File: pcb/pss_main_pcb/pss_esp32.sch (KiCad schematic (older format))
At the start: 17 parts, among them J6 UART_Prog, SW4 Main Encoder Input, SW5 EN, SW6 Boot, U6 ESP32-WROOM-32U, U7 2.8inch_SPI_Module_ILI9341_SK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

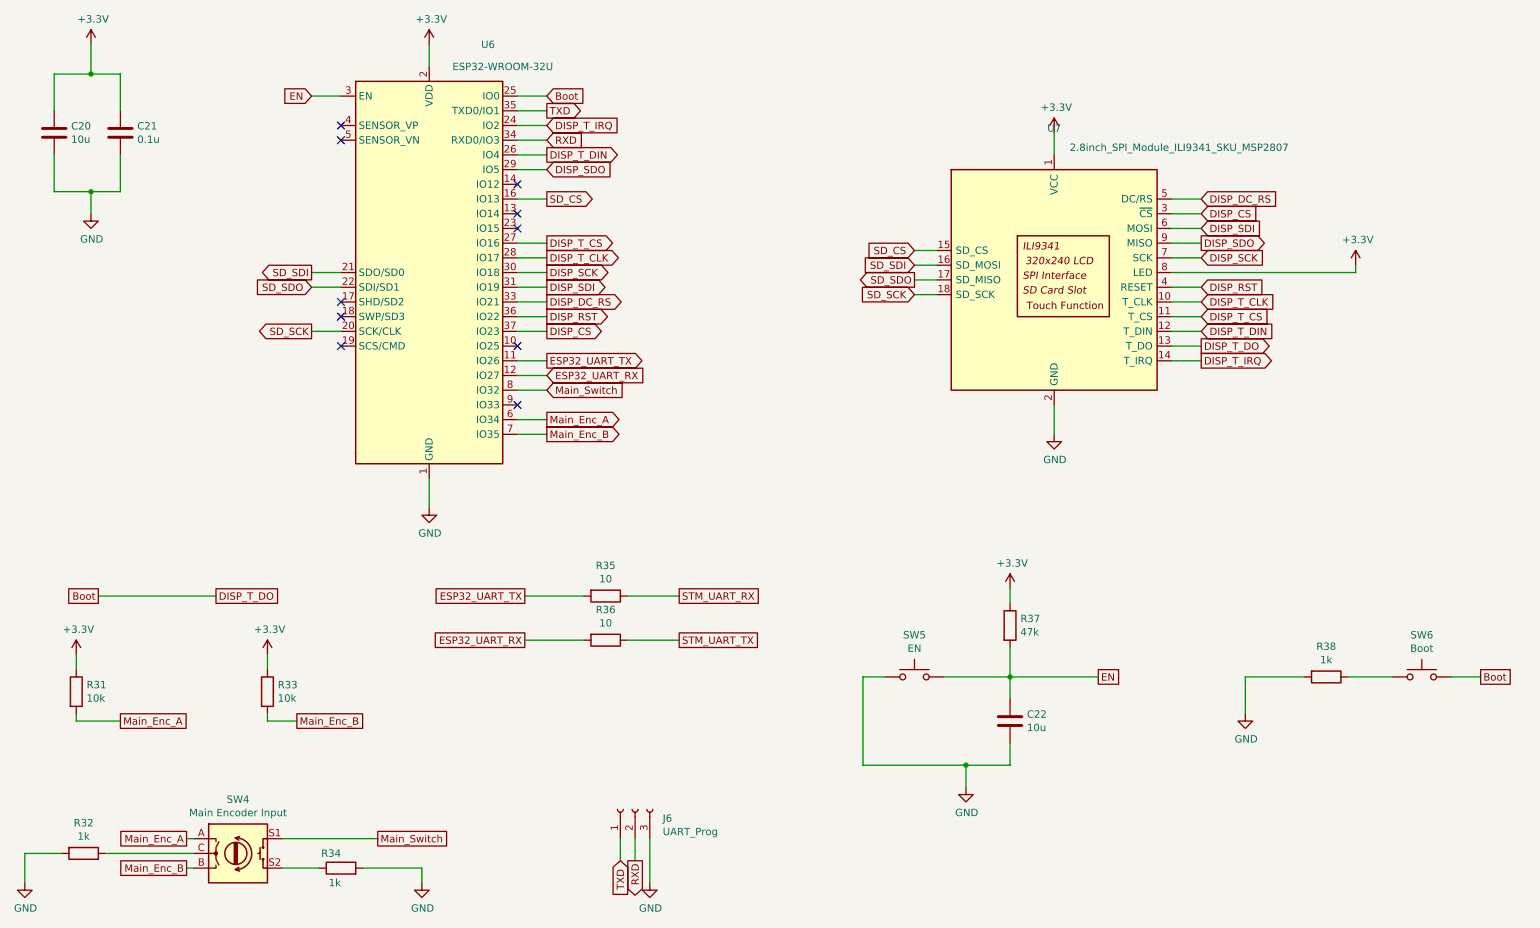
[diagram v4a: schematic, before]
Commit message: Change footprints
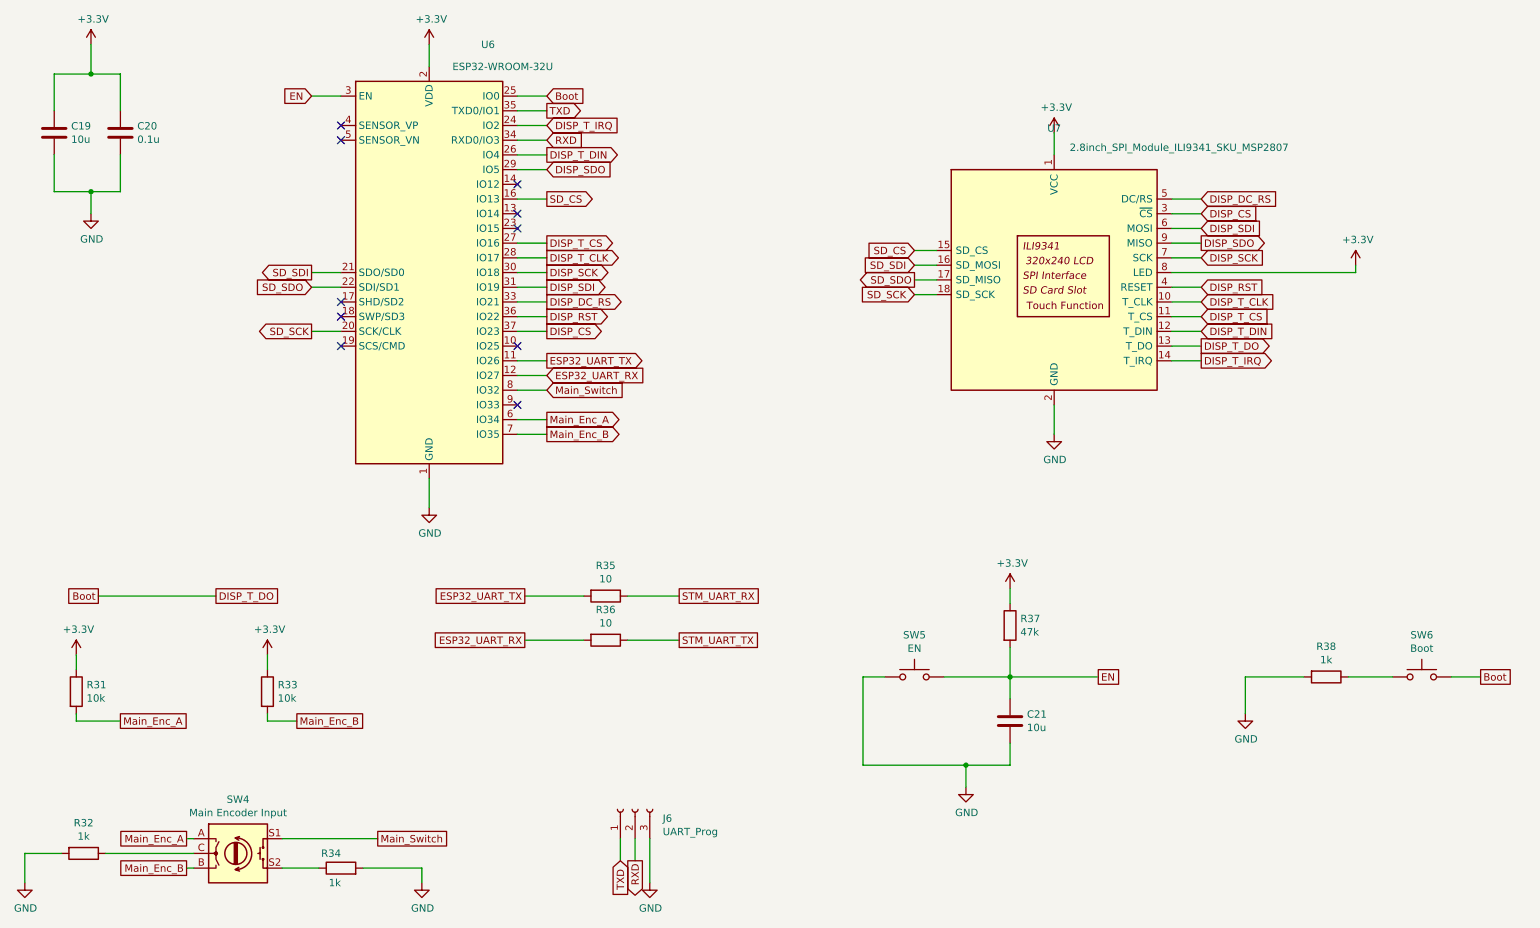
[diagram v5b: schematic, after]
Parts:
- renumbered C20 to C19, C21 to C20, C22 to C21
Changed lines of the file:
@@
 AR Path="/5EE027BC/5ED3F917" Ref="#PWR?"  Part="1"
 AR Path="/5EE5A305/5ED3F917" Ref="#PWR?"  Part="1"
-AR Path="/5ED3D5DF/5ED3F917" Ref="#PWR0147"  Part="1"
-F 0 "#PWR0147" H 750 6600 50  0001 C CNN
+AR Path="/5ED3D5DF/5ED3F917" Ref="#PWR049"  Part="1"
+F 0 "#PWR049" H 750 6600 50  0001 C CNN
 F 1 "GND" H 755 6677 50  0000 C CNN
 F 2 "" H 750 6850 50  0001 C CNN
@@
 AR Path="/5EE027BC/5ED3F923" Ref="#PWR?"  Part="1"
 AR Path="/5EE5A305/5ED3F923" Ref="#PWR?"  Part="1"
-AR Path="/5ED3D5DF/5ED3F923" Ref="#PWR0148"  Part="1"
-F 0 "#PWR0148" H 3450 6600 50  0001 C CNN
+AR Path="/5ED3D5DF/5ED3F923" Ref="#PWR054"  Part="1"
+F 0 "#PWR054" H 3450 6600 50  0001 C CNN
 F 1 "GND" H 3455 6677 50  0000 C CNN
 F 2 "" H 3450 6850 50  0001 C CNN
@@
 	750  6650 1000 6650
 $Comp
-L power:+3.3V #PWR0149
+L power:+3.3V #PWR055
 U 1 1 5ED5E5AE
 P 3500 1150
-F 0 "#PWR0149" H 3500 1000 50  0001 C CNN
+F 0 "#PWR055" H 3500 1000 50  0001 C CNN
 F 1 "+3.3V" H 3515 1323 50  0000 C CNN
 F 2 "" H 3500 1150 50  0001 C CNN
@@
 	3500 1300 3500 1150
 $Comp
-L power:GND #PWR0150
+L power:GND #PWR056
 U 1 1 5ED5F238
 P 3500 4300
-F 0 "#PWR0150" H 3500 4050 50  0001 C CNN
+F 0 "#PWR056" H 3500 4050 50  0001 C CNN
 F 1 "GND" H 3505 4127 50  0000 C CNN
 F 2 "" H 3500 4300 50  0001 C CNN
@@
 P 1200 1150
 AR Path="/5EE5A305/5ED64B6F" Ref="#PWR?"  Part="1"
-AR Path="/5ED3D5DF/5ED64B6F" Ref="#PWR0151"  Part="1"
-F 0 "#PWR0151" H 1200 1000 50  0001 C CNN
+AR Path="/5ED3D5DF/5ED64B6F" Ref="#PWR051"  Part="1"
+F 0 "#PWR051" H 1200 1000 50  0001 C CNN
 F 1 "+3.3V" H 1215 1323 50  0000 C CNN
 F 2 "" H 1200 1150 50  0001 C CNN
@@
 P 950 1750
 AR Path="/5EE5A305/5ED64B77" Ref="C?"  Part="1"
-AR Path="/5ED3D5DF/5ED64B77" Ref="C20"  Part="1"
-F 0 "C20" H 1065 1796 50  0000 L CNN
+AR Path="/5ED3D5DF/5ED64B77" Ref="C19"  Part="1"
+F 0 "C19" H 1065 1796 50  0000 L CNN
 F 1 "10u" H 1065 1705 50  0000 L CNN
 F 2 "Capacitor_SMD:C_1206_3216Metric_Pad1.42x1.75mm_HandSolder" H 988 1600 50  0001 C CNN
@@
 P 1400 1750
 AR Path="/5EE5A305/5ED64B7D" Ref="C?"  Part="1"
-AR Path="/5ED3D5DF/5ED64B7D" Ref="C21"  Part="1"
-F 0 "C21" H 1515 1796 50  0000 L CNN
+AR Path="/5ED3D5DF/5ED64B7D" Ref="C20"  Part="1"
+F 0 "C20" H 1515 1796 50  0000 L CNN
 F 1 "0.1u" H 1515 1705 50  0000 L CNN
 F 2 "Capacitor_SMD:C_1206_3216Metric_Pad1.42x1.75mm_HandSolder" H 1438 1600 50  0001 C CNN
@@
 P 1200 2300
 AR Path="/5EE5A305/5ED64B83" Ref="#PWR?"  Part="1"
-AR Path="/5ED3D5DF/5ED64B83" Ref="#PWR0152"  Part="1"
-F 0 "#PWR0152" H 1200 2050 50  0001 C CNN
+AR Path="/5ED3D5DF/5ED64B83" Ref="#PWR052"  Part="1"
+F 0 "#PWR052" H 1200 2050 50  0001 C CNN
 F 1 "GND" H 1205 2127 50  0000 C CNN
 F 2 "" H 1200 2300 50  0001 C CNN
@@
 	4900 6700 4900 6550
 $Comp
-L power:GND #PWR0153
+L power:GND #PWR057
 U 1 1 5ED730C8
 P 5000 6850
-F 0 "#PWR0153" H 5000 6600 50  0001 C CNN
+F 0 "#PWR057" H 5000 6600 50  0001 C CNN
 F 1 "GND" H 5005 6677 50  0000 C CNN
 F 2 "" H 5000 6850 50  0001 C CNN
@@
 Boot
 $Comp
-L power:GND #PWR0154
+L power:GND #PWR062
 U 1 1 5ED768EF
 P 9050 5700
-F 0 "#PWR0154" H 9050 5450 50  0001 C CNN
+F 0 "#PWR062" H 9050 5450 50  0001 C CNN
 F 1 "GND" H 9055 5527 50  0000 C CNN
 F 2 "" H 9050 5700 50  0001 C CNN
@@
 	9050 5450 9050 5700
 $Comp
-L power:+3.3V #PWR0155
+L power:+3.3V #PWR059
 U 1 1 5ED8CB02
 P 7450 4850
-F 0 "#PWR0155" H 7450 4700 50  0001 C CNN
+F 0 "#PWR059" H 7450 4700 50  0001 C CNN
 F 1 "+3.3V" H 7465 5023 50  0000 C CNN
 F 2 "" H 7450 4850 50  0001 C CNN
@@
 $EndComp
 $Comp
-L Device:C C22
+L Device:C C21
 U 1 1 5ED8F83A
 P 7450 5750
-F 0 "C22" H 7565 5796 50  0000 L CNN
+F 0 "C21" H 7565 5796 50  0000 L CNN
 F 1 "10u" H 7565 5705 50  0000 L CNN
 F 2 "Capacitor_SMD:C_1206_3216Metric_Pad1.42x1.75mm_HandSolder" H 7488 5600 50  0001 C CNN
@@
 $EndComp
 $Comp
-L power:GND #PWR0156
+L power:GND #PWR058
 U 1 1 5ED92F5B
 P 7150 6200
-F 0 "#PWR0156" H 7150 5950 50  0001 C CNN
+F 0 "#PWR058" H 7150 5950 50  0001 C CNN
 F 1 "GND" H 7155 6027 50  0000 C CNN
 F 2 "" H 7150 6200 50  0001 C CNN
@@
 	4100 1800 4300 1800
 $Comp
-L power:GND #PWR0157
+L power:GND #PWR061
 U 1 1 5EDDB701
 P 7750 3800
-F 0 "#PWR0157" H 7750 3550 50  0001 C CNN
+F 0 "#PWR061" H 7750 3550 50  0001 C CNN
 F 1 "GND" H 7755 3627 50  0000 C CNN
 F 2 "" H 7750 3800 50  0001 C CNN
@@
 $EndComp
 $Comp
-L power:+3.3V #PWR0158
+L power:+3.3V #PWR060
 U 1 1 5EDDC5DA
 P 7750 1750
-F 0 "#PWR0158" H 7750 1600 50  0001 C CNN
+F 0 "#PWR060" H 7750 1600 50  0001 C CNN
 F 1 "+3.3V" H 7765 1923 50  0000 C CNN
 F 2 "" H 7750 1750 50  0001 C CNN
@@
 	7750 1900 7750 1750
 $Comp
-L power:+3.3V #PWR0159
+L power:+3.3V #PWR063
 U 1 1 5EDDFD06
 P 9800 2650
-F 0 "#PWR0159" H 9800 2500 50  0001 C CNN
+F 0 "#PWR063" H 9800 2500 50  0001 C CNN
 F 1 "+3.3V" H 9815 2823 50  0000 C CNN
 F 2 "" H 9800 2650 50  0001 C CNN
@@
 	1100 5750 1100 5700
 $Comp
-L power:+3.3V #PWR0160
+L power:+3.3V #PWR050
 U 1 1 5ECE19CC
 P 1100 5300
-F 0 "#PWR0160" H 1100 5150 50  0001 C CNN
+F 0 "#PWR050" H 1100 5150 50  0001 C CNN
 F 1 "+3.3V" H 1115 5473 50  0000 C CNN
 F 2 "" H 1100 5300 50  0001 C CNN
@@
 $EndComp
 $Comp
-L power:+3.3V #PWR0161
+L power:+3.3V #PWR053
 U 1 1 5ECE1EC4
 P 2400 5300
-F 0 "#PWR0161" H 2400 5150 50  0001 C CNN
+F 0 "#PWR053" H 2400 5150 50  0001 C CNN
 F 1 "+3.3V" H 2415 5473 50  0000 C CNN
 F 2 "" H 2400 5300 50  0001 C CNN

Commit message: Add 3D models and totaly redesign PCB
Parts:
- SW4: footprint Rotary_Encoder:RotaryEncoder_Alps_EC11E-Switch_Vertical_H20mm -> encoders:RotaryEncoder_Alps_EC11E-Switch_Vertical_H20mm
- SW5, SW6: footprint Button_Switch_SMD:SW_SPST_B3S-1000 -> buttons:SW_SPST_B3S-1000
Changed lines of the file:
@@
 F 0 "SW4" H 2200 7017 50  0000 C CNN
 F 1 "Main Encoder Input" H 2200 6926 50  0000 C CNN
-F 2 "Rotary_Encoder:RotaryEncoder_Alps_EC11E-Switch_Vertical_H20mm" H 2050 6810 50  0001 C CNN
+F 2 "encoders:RotaryEncoder_Alps_EC11E-Switch_Vertical_H20mm" H 2050 6810 50  0001 C CNN
 F 3 "~" H 2200 6910 50  0001 C CNN
 	1    2200 6650
@@
 F 0 "SW5" H 6800 5735 50  0000 C CNN
 F 1 "EN" H 6800 5644 50  0000 C CNN
-F 2 "Button_Switch_SMD:SW_SPST_B3S-1000" H 6800 5650 50  0001 C CNN
+F 2 "buttons:SW_SPST_B3S-1000" H 6800 5650 50  0001 C CNN
 F 3 "~" H 6800 5650 50  0001 C CNN
 	1    6800 5450
@@
 F 0 "SW6" H 10250 5735 50  0000 C CNN
 F 1 "Boot" H 10250 5644 50  0000 C CNN
-F 2 "Button_Switch_SMD:SW_SPST_B3S-1000" H 10250 5650 50  0001 C CNN
+F 2 "buttons:SW_SPST_B3S-1000" H 10250 5650 50  0001 C CNN
 F 3 "~" H 10250 5650 50  0001 C CNN
 	1    10250 5450
